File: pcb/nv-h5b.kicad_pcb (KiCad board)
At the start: 2 copper layers, 8 x 20 mm, 17 parts, among them J1 PSH02-03, J2 Conn_01x01, J3 Conn_01x01, J4 Conn_01x01, J5 Conn_01x01, J6 Conn_01x01, J7 Conn_01x01, U1 ATtiny25-20SS

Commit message: Silkscreen.
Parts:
- moved J2 0.25 mm to (124.0, 117.6)
- moved J3 0.25 mm to (126.6, 117.6)
- moved J7 0.25 mm to (121.3, 118.1)
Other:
- board text added: "+"
- board text added: "D"
- board text added: "bílá"
- board text added: "zelená"
- board text added: "červ."
- board text added: "žld."
- board text added: "žlhor."
- board text added: "⏚"
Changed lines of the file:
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@@
     (property "Sheetname" "")
     (attr smd)
-    (fp_text reference "D1" (at 0 -2.4 90) (layer "F.SilkS") hide
-      (effects (font (size 1 1) (thickness 0.15)))
+    (fp_text reference "D1" (at 1.27 1.143 180) (layer "F.SilkS") hide
+      (effects (font (size 0.75 0.75) (thickness 0.1)))
     )
     (fp_text value "BAT54" (at 0 2.4 90) (layer "F.Fab")
@@
   )
   (footprint "TestPoint:TestPoint_Keystone_5015_Micro-Minature" (layer "B.Cu")
-    (at 121.285 117.856 -90)
+    (at 121.285 118.11 -90)
     (descr "SMT Test Point- Micro Miniature 5015, http://www.keyelco.com/product-pdf.cfm?p=1353")
     (tags "Test Point")
@@
   )
   (footprint "TestPoint:TestPoint_Keystone_5015_Micro-Minature" (layer "B.Cu")
-    (at 126.619 117.348 -90)
+    (at 126.619 117.602 -90)
     (descr "SMT Test Point- Micro Miniature 5015, http://www.keyelco.com/product-pdf.cfm?p=1353")
     (tags "Test Point")
@@
   )
   (footprint "TestPoint:TestPoint_Keystone_5015_Micro-Minature" (layer "B.Cu")
-    (at 123.952 117.348 -90)
+    (at 123.952 117.602 -90)
     (descr "SMT Test Point- Micro Miniature 5015, http://www.keyelco.com/product-pdf.cfm?p=1353")
     (tags "Test Point")
@@
   (gr_arc (start 128 125.7) (mid 127 124.7) (end 128 123.7) (layer "Edge.Cuts") (width 0.1))
   (gr_line (start 120 130) (end 120 110) (layer "Edge.Cuts") (width 0.1))
+  (gr_text "D" (at 123.952 126.365) (layer "B.SilkS")
+    (effects (font (size 1.5 1.5) (thickness 0.1)) (justify mirror))
+  )
+  (gr_text "⏚" (at 126.492 126.365) (layer "B.SilkS")
+    (effects (font (size 1.5 1.5) (thickness 0.1)) (justify mirror))
+  )
+  (gr_text "červ." (at 121.285 115.189) (layer "B.SilkS")
+    (effects (font (size 0.5 0.5) (thickness 0.1)) (justify mirror))
+  )
+  (gr_text "žlhor." (at 126.619 115.189) (layer "B.SilkS")
+    (effects (font (size 0.5 0.5) (thickness 0.1)) (justify mirror))
+  )
+  (gr_text "žld." (at 123.952 120.142) (layer "B.SilkS")
+    (effects (font (size 0.5 0.5) (thickness 0.1)) (justify mirror))
+  )
+  (gr_text "bílá" (at 126.619 120.142) (layer "B.SilkS")
+    (effects (font (size 0.5 0.5) (thickness 0.1)) (justify mirror))
+  )
+  (gr_text "+" (at 121.412 126.365) (layer "B.SilkS")
+    (effects (font (size 1.5 1.5) (thickness 0.1)) (justify mirror))
+  )
+  (gr_text "+" (at 121.285 120.65) (layer "B.SilkS")
+    (effects (font (size 1 1) (thickness 0.1)) (justify mirror))
+  )
+  (gr_text "zelená" (at 123.952 110.49) (layer "B.SilkS")
+    (effects (font (size 0.5 0.5) (thickness 0.1)) (justify mirror))
+  )
+  (gr_text "⏚" (at 127.127 126.365) (layer "F.SilkS")
+    (effects (font (size 1 1) (thickness 0.1)))
+  )
   (segment (start 121.6175 124.4115) (end 121.158 123.952) (width 0.4) (layer "F.Cu") (net 1))
   (segment (start 121.111 122.428) (end 121.111 123.905) (width 0.4) (layer "F.Cu") (net 1))
@@
   (via (at 121.158 123.952) (size 0.6) (drill 0.3) (layers "F.Cu" "B.Cu") (net 1))
   (segment (start 121.158 123.952) (end 121.285 123.825) (width 0.4) (layer "B.Cu") (net 1))
-  (segment (start 121.285 123.825) (end 121.285 117.856) (width 0.4) (layer "B.Cu") (net 1))
+  (segment (start 121.285 123.825) (end 121.285 118.11) (width 0.4) (layer "B.Cu") (net 1))
   (segment (start 125.476 126.172) (end 125.283 126.172) (width 0.4) (layer "F.Cu") (net 2))
   (segment (start 120.777 124.841) (end 120.235 124.299) (width 0.3) (layer "F.Cu") (net 2))
@@
   (via (at 123.952 122.428) (size 0.6) (drill 0.3) (layers "F.Cu" "B.Cu") (net 5))
   (segment (start 123.952 128.524) (end 123.952 122.428) (width 0.3) (layer "B.Cu") (net 5))
-  (segment (start 123.601893 117.348) (end 123.952 117.348) (width 0.3) (layer "F.Cu") (net 6))
   (segment (start 121.285 115.0385) (end 121.292393 115.0385) (width 0.3) (layer "F.Cu") (net 6))
-  (segment (start 121.292393 115.0385) (end 123.601893 117.348) (width 0.3) (layer "F.Cu") (net 6))
+  (segment (start 123.855893 117.602) (end 123.952 117.602) (width 0.3) (layer "F.Cu") (net 6))
+  (segment (start 121.292393 115.0385) (end 123.855893 117.602) (width 0.3) (layer "F.Cu") (net 6))
   (via (at 123.952 117.348) (size 0.6) (drill 0.3) (layers "F.Cu" "B.Cu") (net 6))
   (segment (start 126.8965 122.428) (end 126.8965 123.5475) (width 0.3) (layer "F.Cu") (net 7))
   (segment (start 126.8965 123.5475) (end 126.746 123.698) (width 0.3) (layer "F.Cu") (net 7))
   (via (at 126.746 123.698) (size 0.6) (drill 0.3) (layers "F.Cu" "B.Cu") (net 7))
-  (segment (start 126.619 123.571) (end 126.619 117.348) (width 0.3) (layer "B.Cu") (net 7))
   (segment (start 126.746 123.698) (end 126.619 123.571) (width 0.3) (layer "B.Cu") (net 7))
+  (segment (start 126.619 123.571) (end 126.619 117.602) (width 0.3) (layer "B.Cu") (net 7))
   (via (at 121.158 111.1015) (size 0.6) (drill 0.3) (layers "F.Cu" "B.Cu") (net 8))
   (segment (start 121.158 112.649) (end 121.285 112.776) (width 0.25) (layer "B.Cu") (net 8))

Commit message: kikit panelize: add tolerance.
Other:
- board text added: "NV-H5b v3.0"
- board text added: "žldol."
- board text removed: "žld."
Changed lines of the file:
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@@
     (effects (font (size 1.5 1.5) (thickness 0.1)) (justify mirror))
+  )
+  (gr_text "NV-H5b\nv3.0" (at 123.952 123.19) (layer "B.SilkS")
+    (effects (font (size 1 1) (thickness 0.1)) (justify mirror))
   )
   (gr_text "červ." (at 121.285 115.189) (layer "B.SilkS")
@@
     (effects (font (size 0.5 0.5) (thickness 0.1)) (justify mirror))
   )
-  (gr_text "žld." (at 123.952 120.142) (layer "B.SilkS")
+  (gr_text "žldol." (at 123.952 120.142) (layer "B.SilkS")
     (effects (font (size 0.5 0.5) (thickness 0.1)) (justify mirror))
   )

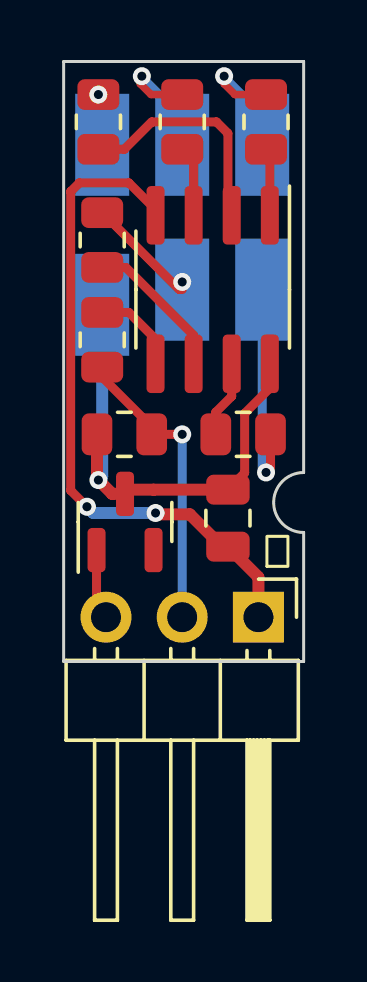
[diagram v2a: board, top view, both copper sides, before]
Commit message: Add part names to silkscreen.
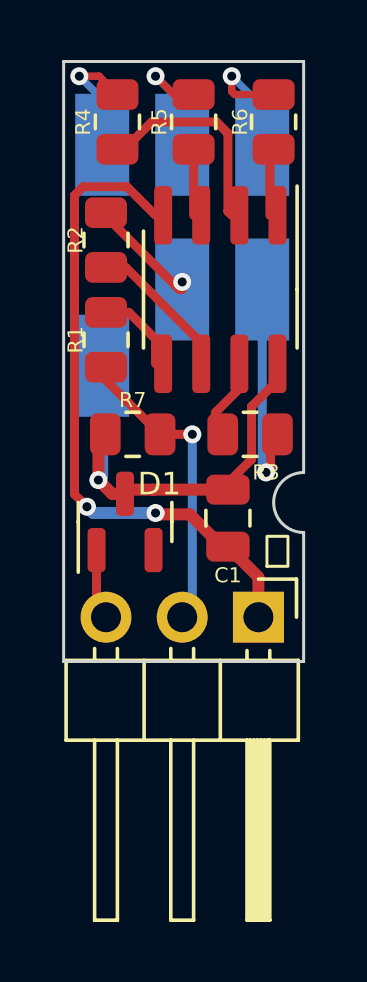
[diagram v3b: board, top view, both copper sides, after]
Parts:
- moved J7 2.03 mm to (121.3, 120.1)
- moved R4 0.64 mm to (121.8, 112.0)
- moved R5 0.38 mm to (124.3, 112.0)
- moved R7 0.28 mm to (122.3, 122.4)
- moved R6 0.25 mm to (127.0, 112.0)
- moved U1 0.25 mm to (125.2, 117.6)
- moved R3 0.23 mm to (126.2, 122.4)
- moved R1 0.13 mm to (121.4, 119.3)
- moved R2 0.13 mm to (121.4, 116.0)
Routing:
- net /LED_RED: track 1.73 -> 5.67 mm
- net VCC: track 16.8 -> 14.9 mm
- net /dLED_RED: track 7.64 -> 7.00 mm

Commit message: Add *.kicad_prl to .gitignore.
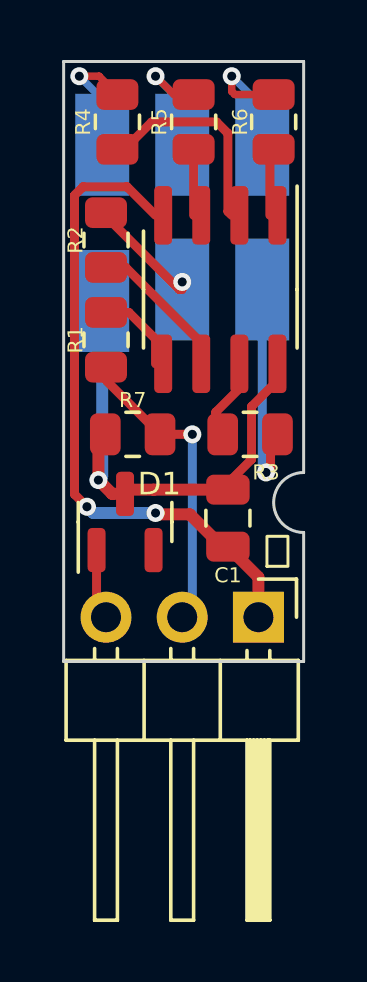
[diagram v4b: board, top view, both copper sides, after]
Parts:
- moved J7 2.16 mm to (121.3, 118.0)
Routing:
- net VCC: track 14.9 -> 17.1 mm
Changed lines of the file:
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@@
   )
   (footprint "TestPoint:TestPoint_Keystone_5015_Micro-Minature" (layer "B.Cu")
-    (at 121.285 120.142 -90)
+    (at 121.285 117.983 -90)
     (descr "SMT Test Point- Micro Miniature 5015, http://www.keyelco.com/product-pdf.cfm?p=1353")
     (tags "Test Point")
@@
   (segment (start 127.127 120.636472) (end 126.2645 121.498972) (width 0.3) (layer "F.Cu") (net 1))
   (via (at 121.158 123.952) (size 0.6) (drill 0.3) (layers "F.Cu" "B.Cu") (net 1))
-  (segment (start 121.285 120.142) (end 121.285 123.825) (width 0.4) (layer "B.Cu") (net 1))
   (segment (start 121.285 123.825) (end 121.158 123.952) (width 0.4) (layer "B.Cu") (net 1))
+  (segment (start 121.285 117.983) (end 121.285 123.825) (width 0.4) (layer "B.Cu") (net 1))
   (segment (start 125.476 126.172) (end 125.283 126.172) (width 0.4) (layer "F.Cu") (net 2))
   (segment (start 120.362 124.426) (end 120.362 114.461) (width 0.3) (layer "F.Cu") (net 2))
